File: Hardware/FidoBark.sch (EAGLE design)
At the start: 22 parts, among them U1 EDISON_CONNECTOR_FULLHEADER, U2 FTS31XS-U, U3 MCP73831

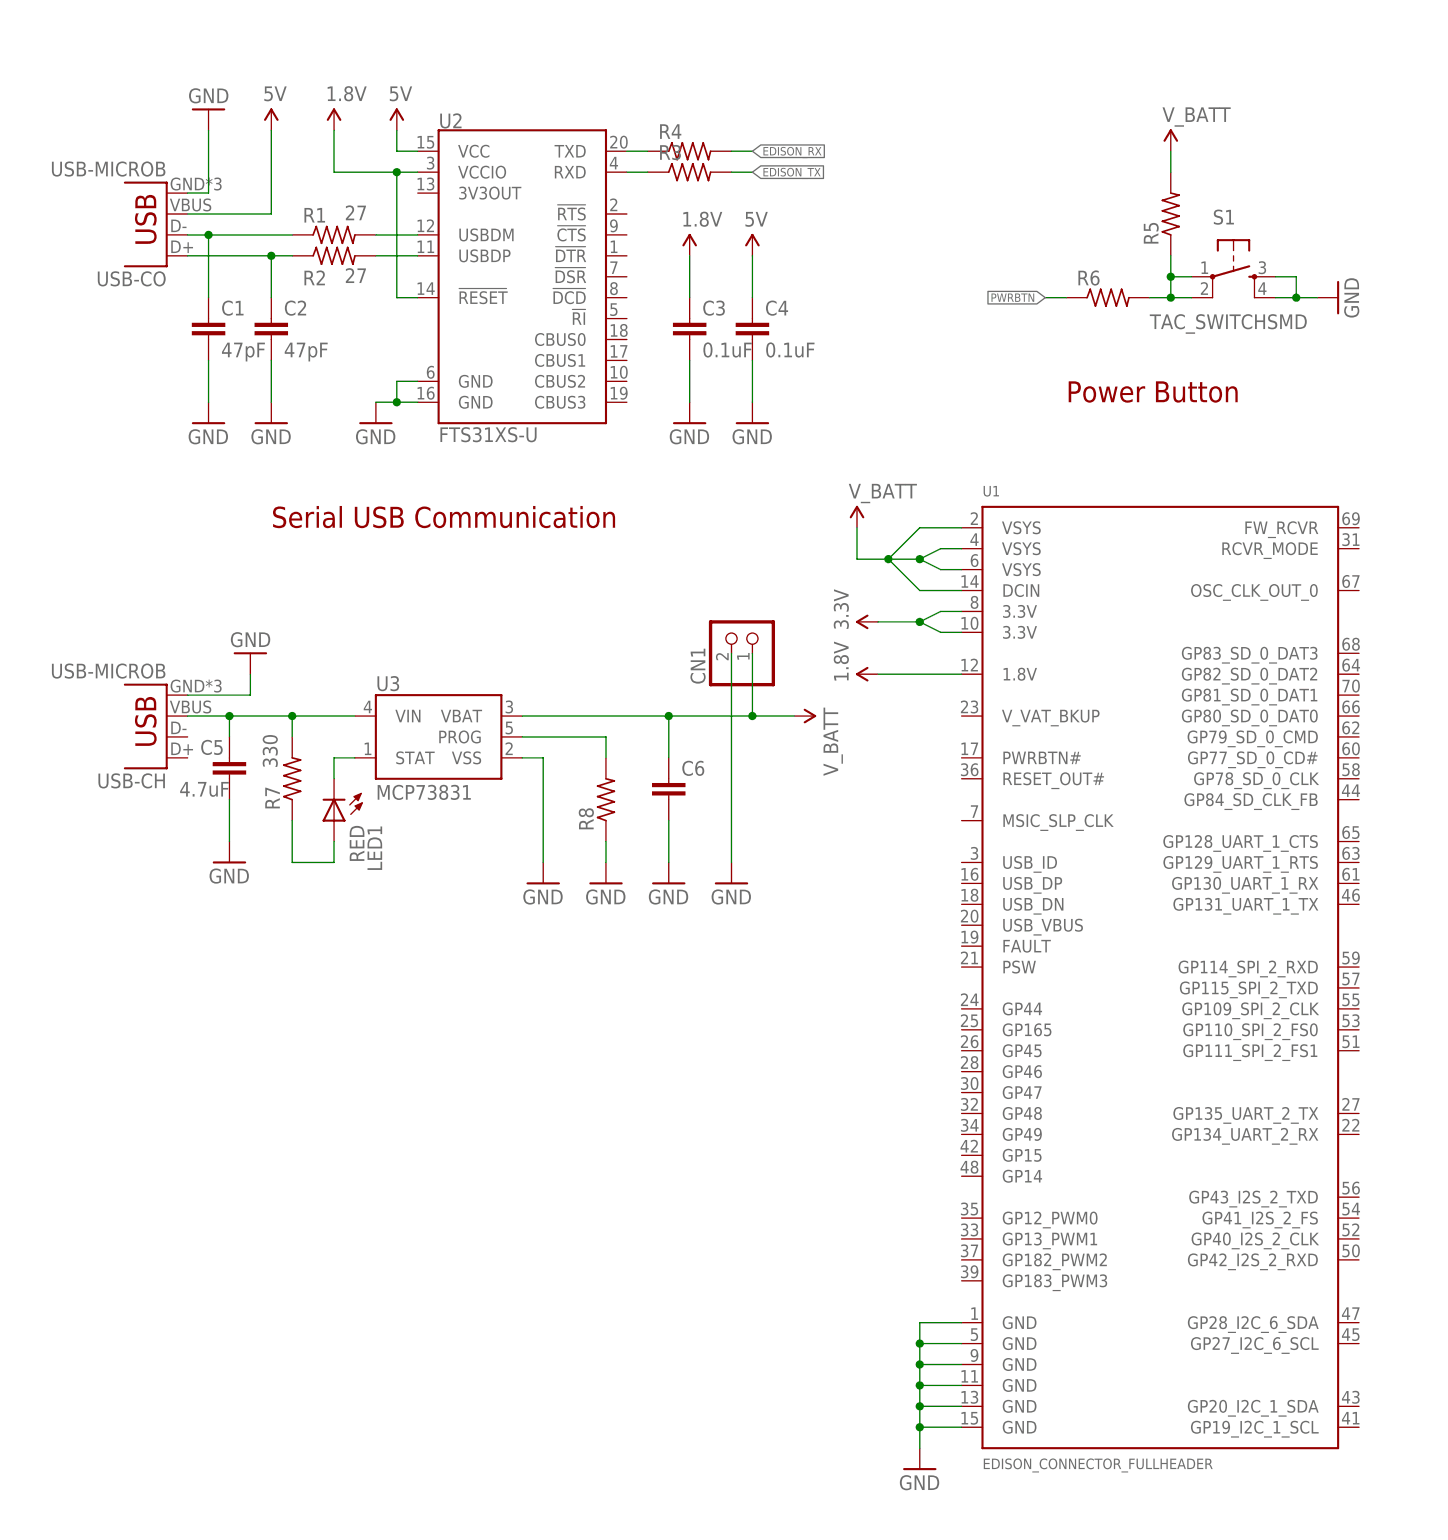
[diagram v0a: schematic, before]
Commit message: motor control
I’m doing the schematic vertically so it can more easily be included
with the paper
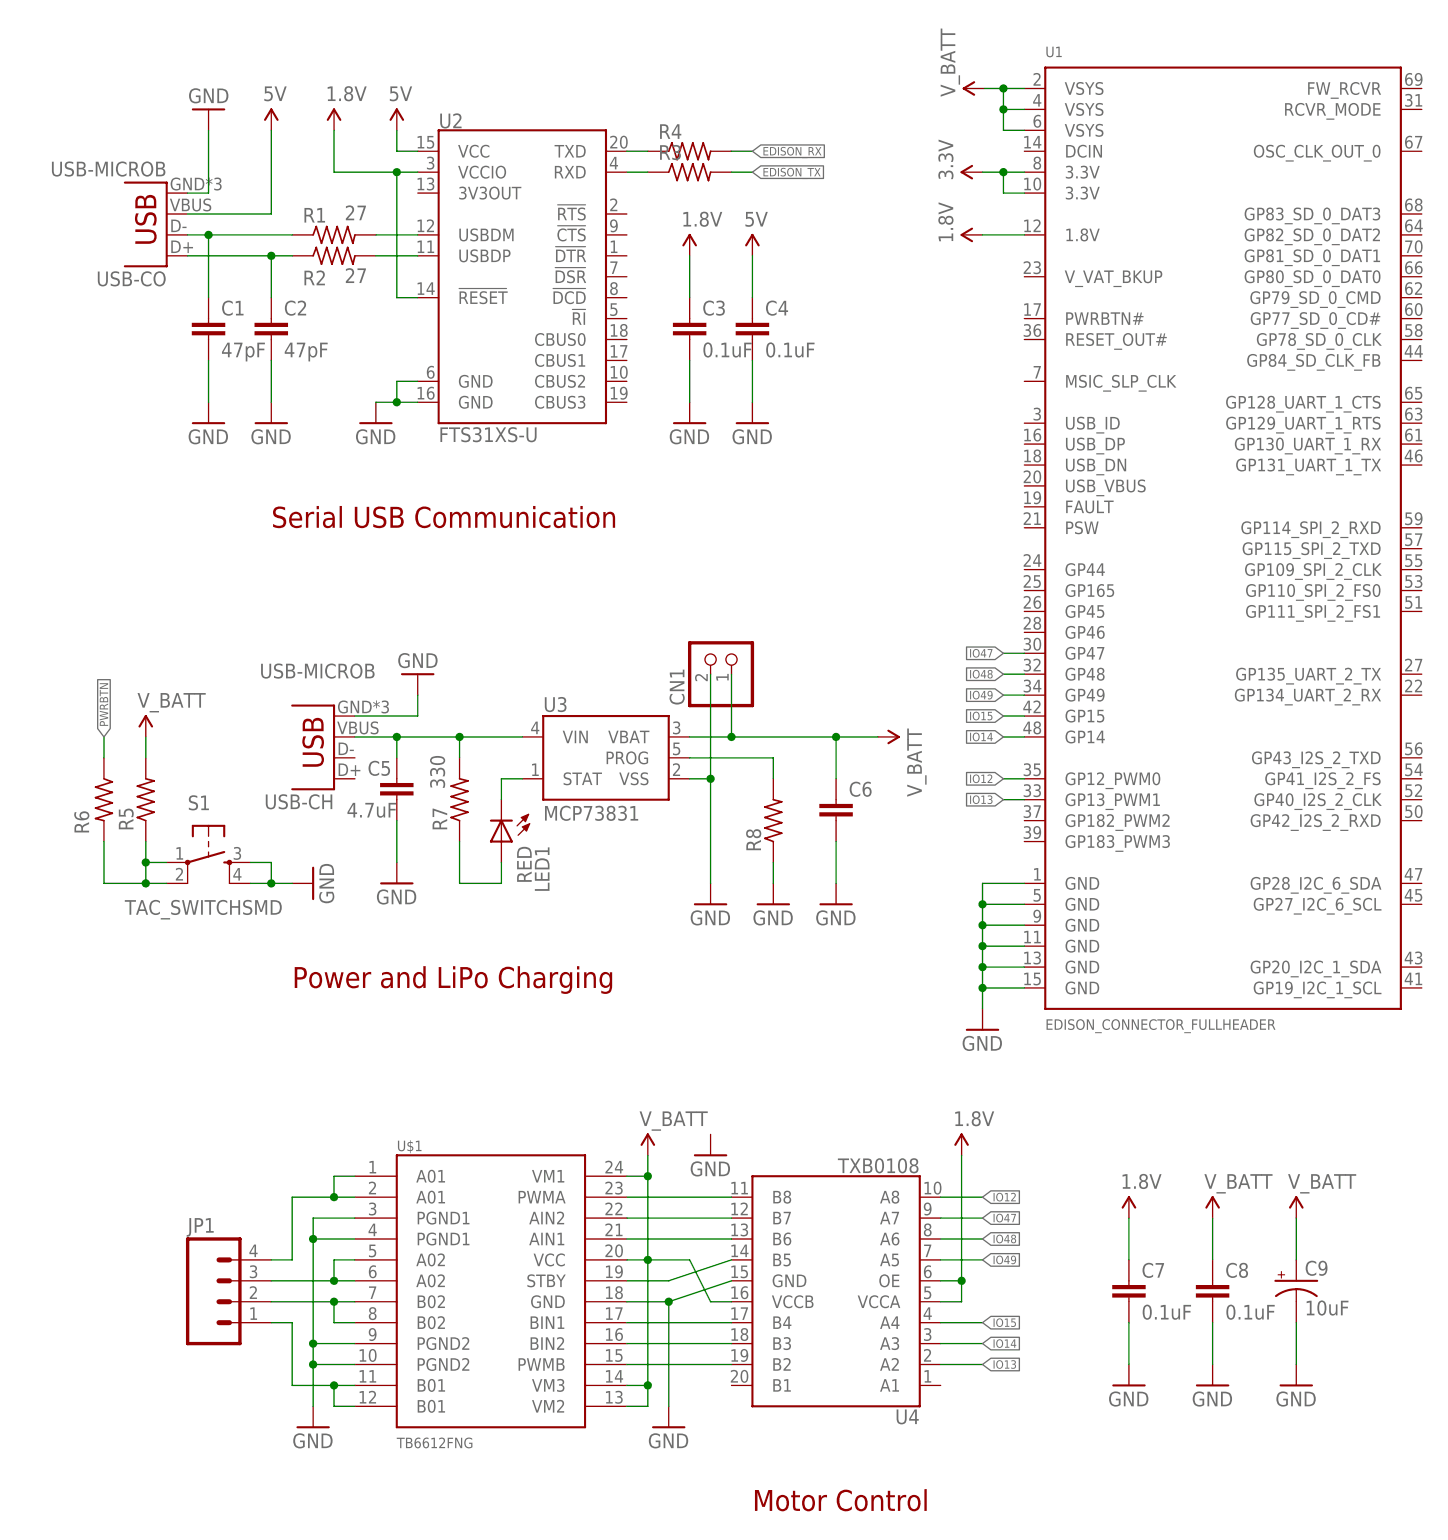
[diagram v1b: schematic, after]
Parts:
- added C7, C8: 0.1uF, SparkFun-Capacitors:CAP0603-CAP
- added C9: 10uF, SparkFun-Capacitors:CAP_POL1206
- added JP1: (no value), SparkFun-Connectors:M04PTH
- added U$1: TB6612FNG, SparkFun-PowerIC:TB6612FNG
- added U4: TXB0108, SparkFun-DigitalIC:TXB0108
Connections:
- new net IO12: U1.GP12_PWM0, U4.A8
- new net IO13: U1.GP13_PWM1, U4.A2
- new net IO14: U1.GP14, U4.A3
- new net IO15: U1.GP15, U4.A4
- new net IO47: U1.GP47, U4.A7
- new net IO48: U1.GP48, U4.A6
- new net IO49: U1.GP49, U4.A5
- new net N$11: JP1.3, U$1.A02@5, U$1.A02@6
- new net N$13: JP1.2, U$1.B02@7, U$1.B02@8
- new net N$15: U$1.PWMA, U4.B8
- new net N$16: U$1.AIN2, U4.B7
- new net N$17: JP1.1, U$1.B01@11, U$1.B01@12
- new net N$18: JP1.4, U$1.A01@1, U$1.A01@2
- new net N$19: U$1.AIN1, U4.B6
- new net N$20: U$1.STBY, U4.B5
- new net N$21: U$1.BIN1, U4.B4
- new net N$22: U$1.BIN2, U4.B3
- new net N$23: U$1.PWMB, U4.B2
- net 1.8V: now also C7.1, U4.OE, U4.VCCA
- net GND: now also C7.2, C8.2, C9.-, U$1.GND, U$1.PGND1@3, U$1.PGND1@4, U$1.PGND2@10, U$1.PGND2@9, U4.GND
- net V_BATT: now also C8.1, C9.+, U$1.VCC, U$1.VM1, U$1.VM2, U$1.VM3, U4.VCCB; no longer U1.DCIN
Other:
- note added: "Motor Control"
- note added: "Power and LiPo Charging"
- note removed: "Power Button"
- moved on the sheet: C5, C6, CN1, LED1, R5, R6, R7, R8, S1, U1, U3, USB-CH

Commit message: adc and organization
now on a3 paper, sorry
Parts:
- added C10, C11, C12: 0.1uF, SparkFun-Passives:CAP0603-CAP
- added JP2: (no value), pinhead:PINHD-1X2
- added R10, R11: 10k, adafruit:R-US_R0603
- added R9: 200k, adafruit:R-US_R0603
- added U5: ADS1015, SparkFun-AnalogIC:ADS1015
- added U6: PCA9306, SparkFun-DigitalIC:PCA9306
- R5: value (none) -> 10k
- R6: value (none) -> 22
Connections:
- new net ADC0: U5.AIN0
- new net ADC1: U5.AIN1
- new net ADC2: U5.AIN2
- new net ADC3: U5.AIN3
- new net N$14: R11.2, U5.ADDR, U5.SCL, U6.SCL2
- new net N$24: R10.2, U5.SDA, U6.SDA2
- new net N$25: R9.2, U6.EN, U6.VREF2
- new net SCL: U6.SCL1
- new net SDA: U6.SDA1
- net 1.8V: now also C10.1, U6.VREF1
- net EDISON_RX: now also U1.GP134_UART_2_RX
- net EDISON_TX: now also U1.GP135_UART_2_TX
- net GND: now also C10.2, C11.2, C12.2, JP2.1, U5.VSS, U6.GND
- net N$12: now also JP2.2
- net PWRBTN: now also U1.PWRBTN#
- net V_BATT: now also C11.1, C12.1, R10.1, R11.1, R9.1, U5.VDD
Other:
- note added: "Analog to Digital Converter"
- note added: "Dual H-Bridge Motor Control"
- note added: "Edison Power Switch"
- note added: "Edison Power and GPIO"
- note added: "USB/Alternate LiPo Charging"
- note removed: "Motor Control"
- note removed: "Power and LiPo Charging"
- moved on the sheet: C1, C2, C3, C4, C5, C6, C7, C8, C9, CN1, JP1, LED1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

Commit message: added sound, light, and temp sensors
I’m a bit worried about running out of analog inputs, and the board
will be a bit difficult to put together: it’s almost all surface mount
components.
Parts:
- added C13: 4.7uF, SparkFun-Passives:CAP0603-CAP
- added C14: 12pF, SparkFun-Passives:CAP0603-CAP
- added C15: 1uF, SparkFun-Passives:CAP0603-CAP
- added R12: PHOTOCELLPTH, SparkFun-Sensors:PHOTOCELLPTH
- added R13, R15, R16, R17: 10k, adafruit:R-US_R0603
- added R14: 2.2k, adafruit:R-US_R0603
- added R18: 1M, adafruit:R-US_R0603
- added U$2: MIC9.7MM, SparkFun-Sensors:MIC9.7MM
- added U$3: OPA344, SparkFun-AnalogIC:OPA344
- added U$4: MCP9700SMD, SparkFun-Sensors:MCP9700SMD
- C6: value (none) -> 4.7uF
- R3, R4: value (none) -> 100
- R8: value (none) -> 2k
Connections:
- new net N$28: C13.1, R14.1, U$2.2
- new net N$29: C13.2, R15.1
- new net N$30: C14.1, R15.2, R18.1, U$3.-IN
- new net N$32: C15.1, R16.1, R17.2, U$3.+IN
- net 3.3V: now also R13.2, R14.2, R16.2, U$3.V+, U$4.VCC
- net ADC0: now also R12.P$2, R13.1
- net ADC1: now also C14.2, R18.2, U$3.OUT
- net ADC2: now also U$4.VO
- net GND: now also C15.2, R12.P$1, R17.1, U$2.1, U$3.V-, U$4.GND
- net SCL: now also U1.GP19_I2C_1_SCL
- net SDA: now also U1.GP20_I2C_1_SDA
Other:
- note added: "Electret Microphone"
- note added: "Temperature"
- note added: "Visible Light"

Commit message: added ir sensor
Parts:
- added R20: 2k, adafruit:R-US_R0603
- added T1: BPX81, opto-trans-siemens:BPX81
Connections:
- net 3.3V: now also T1.C
- net ADC3: now also R20.2, T1.E
- net GND: now also R20.1
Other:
- note added: "Infrared Light"
- moved on the sheet: R12, R13, U$4

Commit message: rev1 complete
current sensors are microphone, temperature,  visible light, ir, 9dof
imu

outputs are motors and a piezo buzzer
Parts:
- added C16, C18: 1uF, SparkFun-Passives:CAP0603-CAP
- added C17: 10uF, SparkFun-Passives:CAP0603-CAP
- added C19: 0.1uF, SparkFun-Passives:CAP0603-CAP
- added C20: 0.22uF, SparkFun-Passives:CAP0603-CAP
- added C21: 4.7uF, SparkFun-Passives:CAP0603-CAP
- added Q1: MMBT2222A, SparkFun-DiscreteSemi:TRANSISTOR_NPNMMBT2222A
- added R19, R21: 10k, adafruit:R-US_R0603
- added R22: 100, adafruit:R-US_R0603
- added SG1: BUZZERSMD2-KIT, SparkFun-Electromechanical:BUZZERSMD2-KIT
- added U7: (no value), SparkFun-PowerIC:MIC52053.3V
- added U8: LSM9DS0, SparkFun-DigitalIC:LSM9DS0
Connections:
- new net IO182: R22.2, U1.GP182_PWM2
- new net N$26: C20.1, U8.SETC
- new net N$27: C20.2, U8.SETP
- new net N$31: C21.1, U8.C1
- new net N$33: R21.1, U8.SDO(G)
- new net N$34: R19.1, U8.SDO(XM)
- new net N$35: Q1.B, R22.1
- new net N$36: Q1.C, SG1.1
- net 1.8V: now also R19.2, R21.2, U8.VDD_IO
- net 3.3V: now also C17.1, C18.1, C19.1, SG1.2, U7.OUT, U8.VDD; no longer U1.3.3V@1, U1.3.3V@2
- net GND: now also C16.2, C17.2, C18.2, C19.2, C21.2, Q1.E, U7.GND, U8.GND
- net SCL: now also U8.SCL
- net SDA: now also U8.SDA
- net V_BATT: now also C16.1, U7.EN, U7.IN
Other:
- note added: "3.3v Voltage Regulation"
- note added: "9dof IMU"
- note added: "FidoBark PCB"
- note added: "Joshua Gruenstein"
- note added: "Michael Truell"
- note added: "Piezo Buzzer"
- note added: "Power Switch"
- note added: "Version 1.0"
- moved on the sheet: R5, R6, S1
